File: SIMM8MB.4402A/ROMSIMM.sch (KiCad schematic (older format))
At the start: 34 parts, among them J1 ROM, U1 MX29LV320, U10 74AHC245, U11 LD1117S33, U2 MX29LV320, U3 74AHC245, U4 74AHC245, U5 74AHC245, U6 74AHC245, U7 74AHC245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

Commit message: 8MB idk
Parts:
- added R1: 3k3, stdpads:R_0805, symbol Device:R_Small
- added SW1: ROM Select, symbol Switch:SW_DIP_x01
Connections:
- net +3V3: now also R1.1
- net GND: now also SW1.2; no longer U1.13 (A21), U2.13 (A21)
- new net RA23: R1.2, SW1.1, U1.13 (A21), U2.13 (A21)
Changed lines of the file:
@@
 Wire Wire Line
 	9600 4400 9600 4300
-Connection ~ 8600 5100
-Wire Wire Line
-	8600 4900 8600 5100
 Text Label 8600 4900 2    50   ~ 0
 RA23
@@
 Wire Wire Line
 	3900 2850 4000 2850
+Text Label 5400 950  2    50   ~ 0
+RA23
+$Comp
+L Device:R_Small R1
+U 1 1 5EC0CD79
+P 5500 850
+F 0 "R1" H 5559 896 50  0000 L CNN
+F 1 "3k3" H 5559 805 50  0000 L CNN
+F 2 "stdpads:R_0805" H 5500 850 50  0001 C CNN
+F 3 "~" H 5500 850 50  0001 C CNN
+	1    5500 850
+	1    0    0    -1
+$EndComp
+Wire Wire Line
+	5400 950  5500 950
+$Comp
+L power:+3V3 #PWR?
+U 1 1 5EC0FA8C
+P 5500 750
+F 0 "#PWR?" H 5500 600 50  0001 C CNN
+F 1 "+3V3" H 5500 900 50  0000 C CNN
+F 2 "" H 5500 750 50  0001 C CNN
+F 3 "" H 5500 750 50  0001 C CNN
+	1    5500 750
+	-1   0    0    -1
+$EndComp
+$Comp
+L Switch:SW_DIP_x01 SW1
+U 1 1 5EC10C6B
+P 5900 950
+F 0 "SW1" H 5900 1100 50  0000 C CNN
+F 1 "ROM Select" H 5900 800 50  0000 C CNN
+F 2 "" H 5900 950 50  0001 C CNN
+F 3 "~" H 5900 950 50  0001 C CNN
+	1    5900 950
+	1    0    0    -1
+$EndComp
+Wire Wire Line
+	5500 950  5600 950
+Connection ~ 5500 950
+$Comp
+L power:GND #PWR?
+U 1 1 5EC13E25
+P 6200 950
+F 0 "#PWR?" H 6200 700 50  0001 C CNN
+F 1 "GND" H 6200 800 50  0000 C CNN
+F 2 "" H 6200 950 50  0001 C CNN
+F 3 "" H 6200 950 50  0001 C CNN
+	1    6200 950
+	-1   0    0    -1
+$EndComp
 $EndSCHEMATC

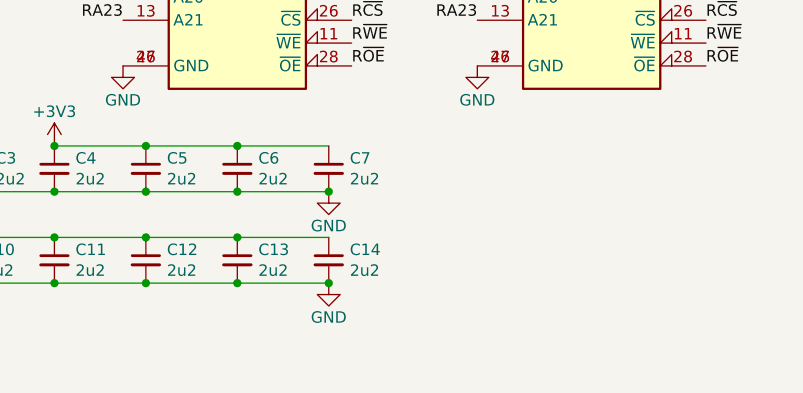
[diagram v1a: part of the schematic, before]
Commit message: 8MB SIMM as sent to JLCPCB June 2020
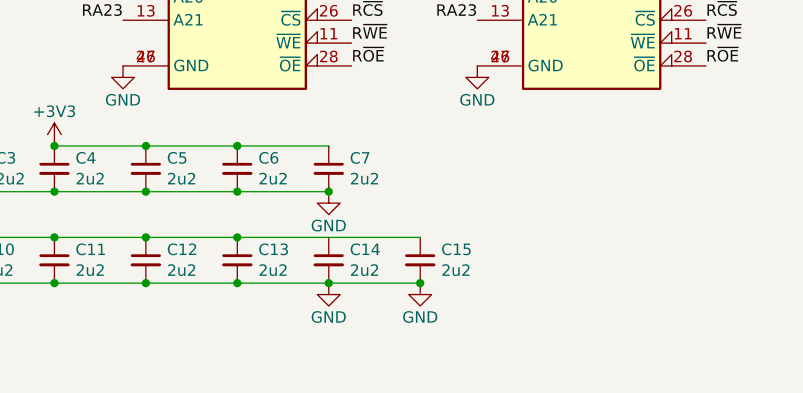
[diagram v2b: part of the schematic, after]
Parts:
- added C15: 2u2, stdpads:C_0603, symbol Device:C_Small
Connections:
- net +3V3: now also C15.1
- net GND: now also C15.2
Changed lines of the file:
@@
 	3800 2650 3900 2650
 $Comp
-L power:GND #PWR?
+L power:GND #PWR0131
 U 1 1 5EC5BB53
 P 3800 2650
-F 0 "#PWR?" H 3800 2400 50  0001 C CNN
+F 0 "#PWR0131" H 3800 2400 50  0001 C CNN
 F 1 "GND" H 3800 2500 50  0000 C CNN
 F 2 "" H 3800 2650 50  0001 C CNN
@@
 	5400 950  5500 950
 $Comp
-L power:+3V3 #PWR?
+L power:+3V3 #PWR0151
 U 1 1 5EC0FA8C
 P 5500 750
-F 0 "#PWR?" H 5500 600 50  0001 C CNN
+F 0 "#PWR0151" H 5500 600 50  0001 C CNN
 F 1 "+3V3" H 5500 900 50  0000 C CNN
 F 2 "" H 5500 750 50  0001 C CNN
@@
 Connection ~ 5500 950
 $Comp
-L power:GND #PWR?
+L power:GND #PWR0152
 U 1 1 5EC13E25
 P 6200 950
-F 0 "#PWR?" H 6200 700 50  0001 C CNN
+F 0 "#PWR0152" H 6200 700 50  0001 C CNN
 F 1 "GND" H 6200 800 50  0000 C CNN
 F 2 "" H 6200 950 50  0001 C CNN
@@
 	-1   0    0    -1
 $EndComp
+$Comp
+L power:GND #PWR0153
+U 1 1 A08D2337
+P 8350 6050
+F 0 "#PWR0153" H 8350 5800 50  0001 C CNN
+F 1 "GND" H 8350 5900 50  0000 C CNN
+F 2 "" H 8350 6050 50  0001 C CNN
+F 3 "" H 8350 6050 50  0001 C CNN
+	1    8350 6050
+	1    0    0    -1
+$EndComp
+Wire Wire Line
+	7950 5850 8350 5850
+Wire Wire Line
+	7950 6050 8350 6050
+$Comp
+L Device:C_Small C15
+U 1 1 A08D233F
+P 8350 5950
+F 0 "C15" H 8442 5996 50  0000 L CNN
+F 1 "2u2" H 8442 5905 50  0000 L CNN
+F 2 "stdpads:C_0603" H 8350 5950 50  0001 C CNN
+F 3 "~" H 8350 5950 50  0001 C CNN
+	1    8350 5950
+	1    0    0    -1
+$EndComp
+Connection ~ 8350 6050
 $EndSCHEMATC

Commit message: 8MB fixes
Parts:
- added R2: 100, stdpads:R_0805, symbol Device:R_Small
- added U12: 74LVC1G02GW, stdpads:SOT-353, symbol GW_Logic:741G02GW
- SW1: footprint (none) -> Button_Switch_SMD:SW_DIP_SPSTx01_Slide_6.7x4.1mm_W8.61mm_P2.54mm_LowProfile
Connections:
- net +3V3: now also U12.5 (Vcc)
- net GND: now also U12.3 (GND)
- net ~CS~: now also U12.1 (B)
- net ~OE~: now also U12.2 (A)
- net ~WE~: no longer U3.1 (AtoB), U4.1 (AtoB), U5.1 (AtoB), U6.1 (AtoB)
- new net Ddir: R2.2, U12.4 (Y), U3.1 (AtoB), U4.1 (AtoB)
- new net DdirR: R2.1, U5.1 (AtoB), U6.1 (AtoB)
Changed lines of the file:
@@
 $EndComp
 Text Label 3400 5350 0    50   ~ 0
-~WE~
+DdirR
 $Comp
 L GW_Logic:74245 U5
@@
 $EndComp
 Text Label 3400 4050 0    50   ~ 0
-~WE~
+DdirR
 $Comp
 L GW_Logic:74245 U4
@@
 $EndComp
 Text Label 3400 2750 0    50   ~ 0
-~WE~
+Ddir
 $Comp
 L GW_Logic:74245 U3
@@
 $EndComp
 Text Label 3400 1450 0    50   ~ 0
-~WE~
+Ddir
 Text Label 3400 4850 0    50   ~ 0
 RD16
@@
 F 0 "SW1" H 5900 1100 50  0000 C CNN
 F 1 "ROM Select" H 5900 800 50  0000 C CNN
-F 2 "" H 5900 950 50  0001 C CNN
+F 2 "Button_Switch_SMD:SW_DIP_SPSTx01_Slide_6.7x4.1mm_W8.61mm_P2.54mm_LowProfile" H 5900 950 50  0001 C CNN
 F 3 "~" H 5900 950 50  0001 C CNN
 	1    5900 950
@@
 $EndComp
 Connection ~ 8350 6050
+$Comp
+L GW_Logic:741G02GW U12
+U 1 1 5EF4BDF5
+P 5700 3250
+F 0 "U12" H 5700 3500 50  0000 C CNN
+F 1 "74LVC1G02GW" H 5700 3000 50  0000 C CNN
+F 2 "stdpads:SOT-353" H 5700 2950 50  0001 C TNN
+F 3 "" H 5700 3050 60  0001 C CNN
+	1    5700 3250
+	1    0    0    -1
+$EndComp
+Text Label 5300 3150 2    50   ~ 0
+~CS~
+$Comp
+L power:+3V3 #PWR0154
+U 1 1 5EF4CD76
+P 6100 3150
+F 0 "#PWR0154" H 6100 3000 50  0001 C CNN
+F 1 "+3V3" H 6100 3300 50  0000 C CNN
+F 2 "" H 6100 3150 50  0001 C CNN
+F 3 "" H 6100 3150 50  0001 C CNN
+	1    6100 3150
+	-1   0    0    -1
+$EndComp
+$Comp
+L power:GND #PWR0155
+U 1 1 5EF4D490
+P 5300 3350
+F 0 "#PWR0155" H 5300 3100 50  0001 C CNN
+F 1 "GND" H 5300 3200 50  0000 C CNN
+F 2 "" H 5300 3350 50  0001 C CNN
+F 3 "" H 5300 3350 50  0001 C CNN
+	1    5300 3350
+	-1   0    0    -1
+$EndComp
+Text Label 6500 3350 0    50   ~ 0
+DdirR
+Text Label 5300 3250 2    50   ~ 0
+~OE~
+$Comp
+L Device:R_Small R2
+U 1 1 5EFDEB5D
+P 6400 3350
+F 0 "R2" V 6350 3350 50  0000 C BNN
+F 1 "100" V 6450 3350 50  0000 C TNN
+F 2 "stdpads:R_0805" H 6400 3350 50  0001 C CNN
+F 3 "~" H 6400 3350 50  0001 C CNN
+	1    6400 3350
+	0    1    1    0
+$EndComp
+Text Label 6100 3350 0    50   ~ 0
+Ddir
+Wire Wire Line
+	6100 3350 6300 3350
 $EndSCHEMATC
